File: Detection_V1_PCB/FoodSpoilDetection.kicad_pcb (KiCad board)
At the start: 2 copper layers, 60 x 65.2 mm, 44 parts, among them J1 Conn_01x03_Socket, J2 Conn_01x04_Socket, J3 Conn_01x06_Socket, J4 Conn_01x03_Socket, J5 Conn_01x10_Socket, J6 Conn_01x03_Socket, Q1 AO3401A, Q2 AO3400A, Q3 AO3401A, SW1 SW_DIP_x01, U1 XIAO-ESP32-S3-DIP

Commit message: measurements
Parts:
- moved FID1 1.30 mm to (134.1, 131.7)
- moved H2 1.15 mm to (178.1, 73.7)
- moved FID2 0.90 mm to (134.4, 71.3)
- moved H4 0.74 mm to (178.8, 130.0)
- moved GND1 0.57 mm to (161.8, 74.0)
- moved FID3 0.38 mm to (173.1, 131.8)
- moved TP1 0.28 mm to (167.4, 73.8)
- moved H1 0.25 mm to (129.0, 73.8)
- moved H3 0.22 mm to (128.8, 130.2)
- moved SW1 0.20 mm to (163.1, 132.3)
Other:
- board size 60 x 65.2 mm -> 60 x 65 mm
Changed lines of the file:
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@@
 	(footprint "MountingHole:MountingHole_3.2mm_M3_Pad_TopBottom"
 		(layer "F.Cu")
-		(at 129 130.2)
+		(at 128.778 130.175)
 		(descr "Mounting Hole 3.2mm, M3, generated by kicad-footprint-generator mountinghole.py")
 		(tags "mountinghole M3")
@@
 	(footprint "Fiducial:Fiducial_1.5mm_Mask3mm"
 		(layer "F.Cu")
-		(at 173.4 131.6)
+		(at 173.101 131.84)
 		(descr "Fiducial, circular marking, 1.5mm bare copper, 3mm soldermask opening")
 		(tags "fiducial")
@@
 	(footprint "MountingHole:MountingHole_3.2mm_M3_Pad_TopBottom"
 		(layer "F.Cu")
-		(at 129.2 73.6)
+		(at 129.032 73.787)
 		(descr "Mounting Hole 3.2mm, M3, generated by kicad-footprint-generator mountinghole.py")
 		(tags "mountinghole M3")
@@
 	(footprint "Fiducial:Fiducial_1.5mm_Mask3mm"
 		(layer "F.Cu")
-		(at 135.2 71.6)
+		(at 134.36 71.27)
 		(descr "Fiducial, circular marking, 1.5mm bare copper, 3mm soldermask opening")
 		(tags "fiducial")
@@
 	(footprint "TestPoint:TestPoint_Loop_D1.80mm_Drill1.0mm_Beaded"
 		(layer "F.Cu")
-		(at 167.6 73.6)
+		(at 167.4 73.8)
 		(descr "wire loop with bead as test point, loop diameter 1.8mm, hole diameter 1.0mm")
 		(tags "test point wire loop bead")
@@
 	(footprint "MountingHole:MountingHole_3.2mm_M3_Pad_TopBottom"
 		(layer "F.Cu")
-		(at 179.2 73.6)
+		(at 178.054 73.67)
 		(descr "Mounting Hole 3.2mm, M3, generated by kicad-footprint-generator mountinghole.py")
 		(tags "mountinghole M3")
@@
 	(footprint "MountingHole:MountingHole_3.2mm_M3_Pad_TopBottom"
 		(layer "F.Cu")
-		(at 179.4 129.6)
+		(at 178.816 130.048)
 		(descr "Mounting Hole 3.2mm, M3, generated by kicad-footprint-generator mountinghole.py")
 		(tags "mountinghole M3")
@@
 	(footprint "Fiducial:Fiducial_1.5mm_Mask3mm"
 		(layer "F.Cu")
-		(at 135.4 131.8)
+		(at 134.1 131.73)
 		(descr "Fiducial, circular marking, 1.5mm bare copper, 3mm soldermask opening")
 		(tags "fiducial")
@@
 	(footprint "TestPoint:TestPoint_Loop_D1.80mm_Drill1.0mm_Beaded"
 		(layer "F.Cu")
-		(at 161.4 73.6)
+		(at 161.8 74)
 		(descr "wire loop with bead as test point, loop diameter 1.8mm, hole diameter 1.0mm")
 		(tags "test point wire loop bead")
@@
 	(footprint "Button_Switch_SMD:SW_SPDT_PCM12"
 		(layer "F.Cu")
-		(at 163.1 132.47)
+		(at 163.1 132.27)
 		(descr "Ultraminiature Surface Mount Slide Switch, right-angle, https://www.ckswitches.com/media/1424/pcm.pdf")
 		(property "Reference" "SW1"
@@
 	)
 	(gr_rect
-		(start 123.92 68.96)
-		(end 183.92 134.16)
+		(start 124 68.9)
+		(end 184 133.9)
 		(stroke
 			(width 0.05)
@@
 		(layer "Edge.Cuts")
 	)
+	(dimension
+		(type orthogonal)
+		(layer "F.Cu")
+		(pts
+			(xy 178.816 129.6) (xy 183.896 129.6)
+		)
+		(height 9.973)
+		(orientation 0)
+		(format
+			(prefix "")
+			(suffix "")
+			(units 3)
+			(units_format 0)
+			(precision 4)
+			(suppress_zeroes yes)
+		)
+		(style
+			(thickness 0.2)
+			(arrow_length 1.27)
+			(text_position_mode 0)
+			(arrow_direction outward)
+			(extension_height 0.58642)
+			(extension_offset 0.5)
+			(keep_text_aligned yes)
+		)
+		(gr_text "0.2"
+			(at 181.356 137.773 0)
+			(layer "F.Cu")
+			(effects
+				(font
+					(size 1.5 1.5)
+					(thickness 0.3)
+				)
+			)
+		)
+	)
+	(dimension
+		(type orthogonal)
+		(layer "F.Cu")
+		(pts
+			(xy 123.92 68.96) (xy 183.92 68.96)
+		)
+		(height -7.96)
+		(orientation 0)
+		(format
+			(prefix "")
+			(suffix "")
+			(units 3)
+			(units_format 0)
+			(precision 4)
+			(suppress_zeroes yes)
+		)
+		(style
+			(thickness 0.2)
+			(arrow_length 1.27)
+			(text_position_mode 0)
+			(arrow_direction outward)
+			(extension_height 0.58642)
+			(extension_offset 0.5)
+			(keep_text_aligned yes)
+		)
+		(gr_text "2.3622"
+			(at 153.92 59.2 0)
+			(layer "F.Cu")
+			(effects
+				(font
+					(size 1.5 1.5)
+					(thickness 0.3)
+				)
+			)
+		)
+	)
+	(dimension
+		(type orthogonal)
+		(layer "F.Cu")
+		(pts
+			(xy 183.92 68.96) (xy 183.92 134.16)
+		)
+		(height 9.68)
+		(orientation 1)
+		(format
+			(prefix "")
+			(suffix "")
+			(units 3)
+			(units_format 0)
+			(precision 4)
+			(suppress_zeroes yes)
+		)
+		(style
+			(thickness 0.2)
+			(arrow_length 1.27)
+			(text_position_mode 0)
+			(arrow_direction outward)
+			(extension_height 0.58642)
+			(extension_offset 0.5)
+			(keep_text_aligned yes)
+		)
+		(gr_text "2.5669"
+			(at 191.8 101.56 90)
+			(layer "F.Cu")
+			(effects
+				(font
+					(size 1.5 1.5)
+					(thickness 0.3)
+				)
+			)
+		)
+	)
 	(segment

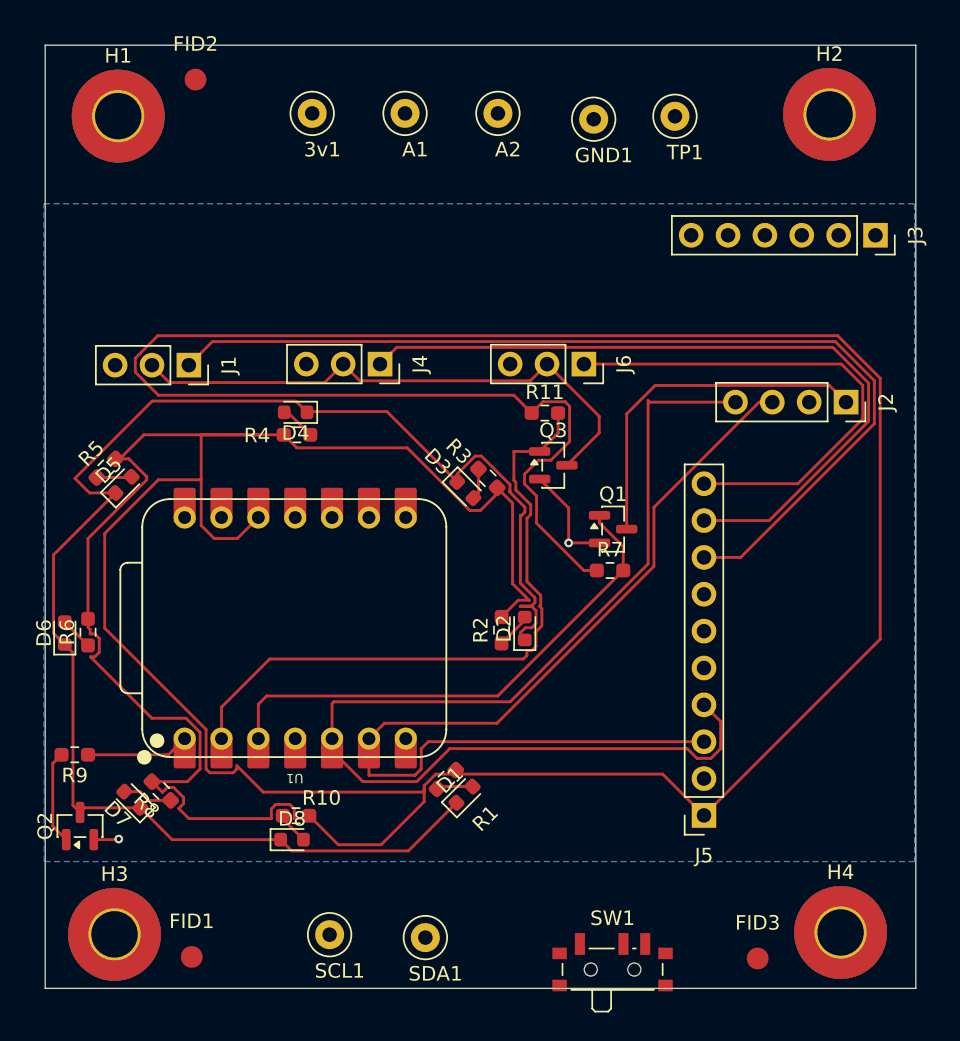
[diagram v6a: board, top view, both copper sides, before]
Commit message: traces to mounting holes and edits to rounting
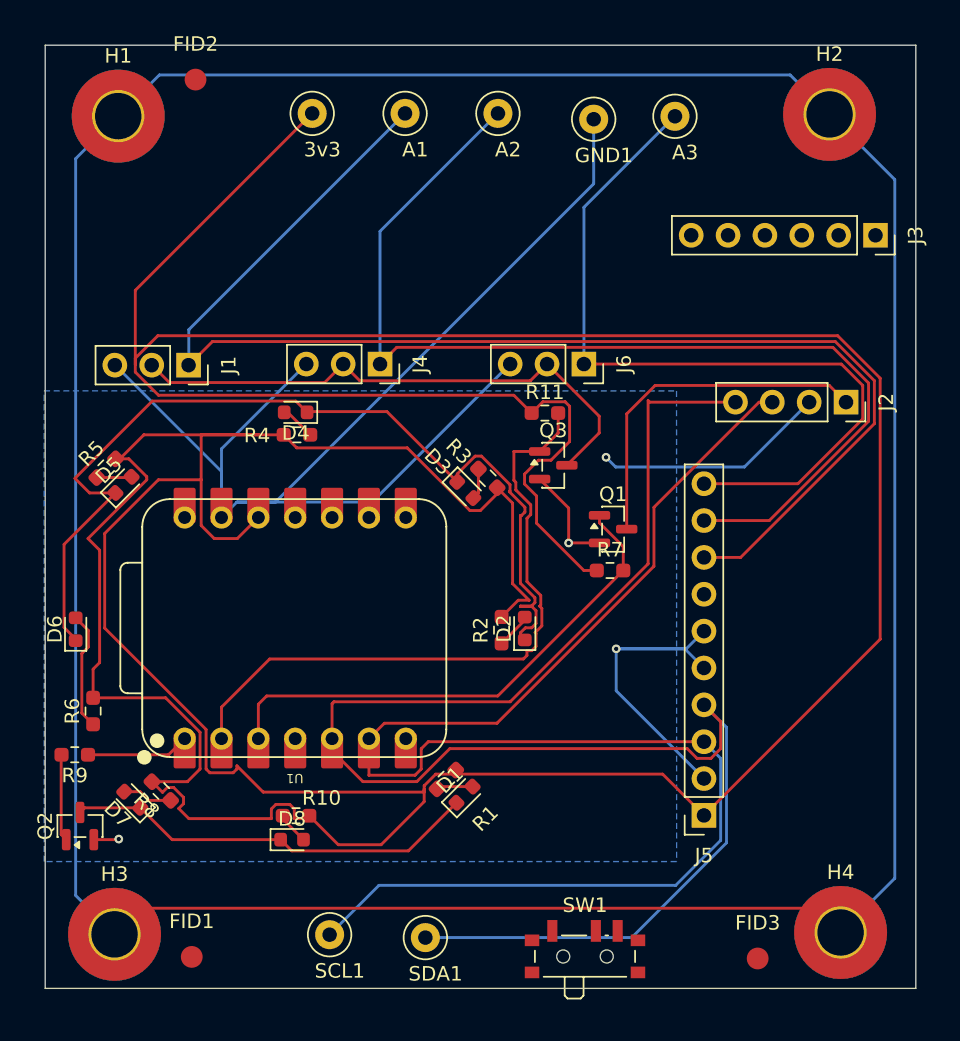
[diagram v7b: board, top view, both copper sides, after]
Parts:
- A3: renamed from TP1; value A3 -> TestPoint
- moved R6 5.45 mm to (127.3, 114.8)
- moved SW1 2.10 mm to (161.2, 131.4)
- moved D6 0.79 mm to (126.1, 109.2)
- renumbered 3v1 to 3v3
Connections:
- Q1 pad 1: D0 -> D2
- R7 pad 2: D0 -> D2
- R9 pad 1: D2 -> D0
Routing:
- net GNDPWR: track 0.00 -> 226.1 mm
- net GND: track 9.31 -> 139.0 mm, vias 2 -> 4
- net SCL: track 66.3 -> 103.3 mm
- net SDA: track 78.1 -> 111.7 mm
- net /A1: track 67.6 -> 91.1 mm
- net 3v3: track 316.7 -> 340.1 mm
- net /A2: track 52.0 -> 72.6 mm
- net /A3: track 34.9 -> 54.6 mm
- net Net-(D1-K): track 107.6 -> 95.0 mm
- net Net-(D6-A): track 2.30 -> 8.18 mm

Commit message: Changes to PCB
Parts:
- removed SW1: SW_DIP_x01, Button_Switch_SMD:SW_SPDT_PCM12
- moved J4 0.35 mm to (147.4, 90.8)
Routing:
- net GND: track 139.0 -> 124.2 mm
- net 3v3: track 340.1 -> 340.9 mm
